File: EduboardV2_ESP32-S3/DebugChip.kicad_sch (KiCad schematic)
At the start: 31 parts, among them Q1 L8050QLT1G, Q2 L8050QLT1G, Q3 AO3401A, U2 CP2102N-A02-GQFN28R

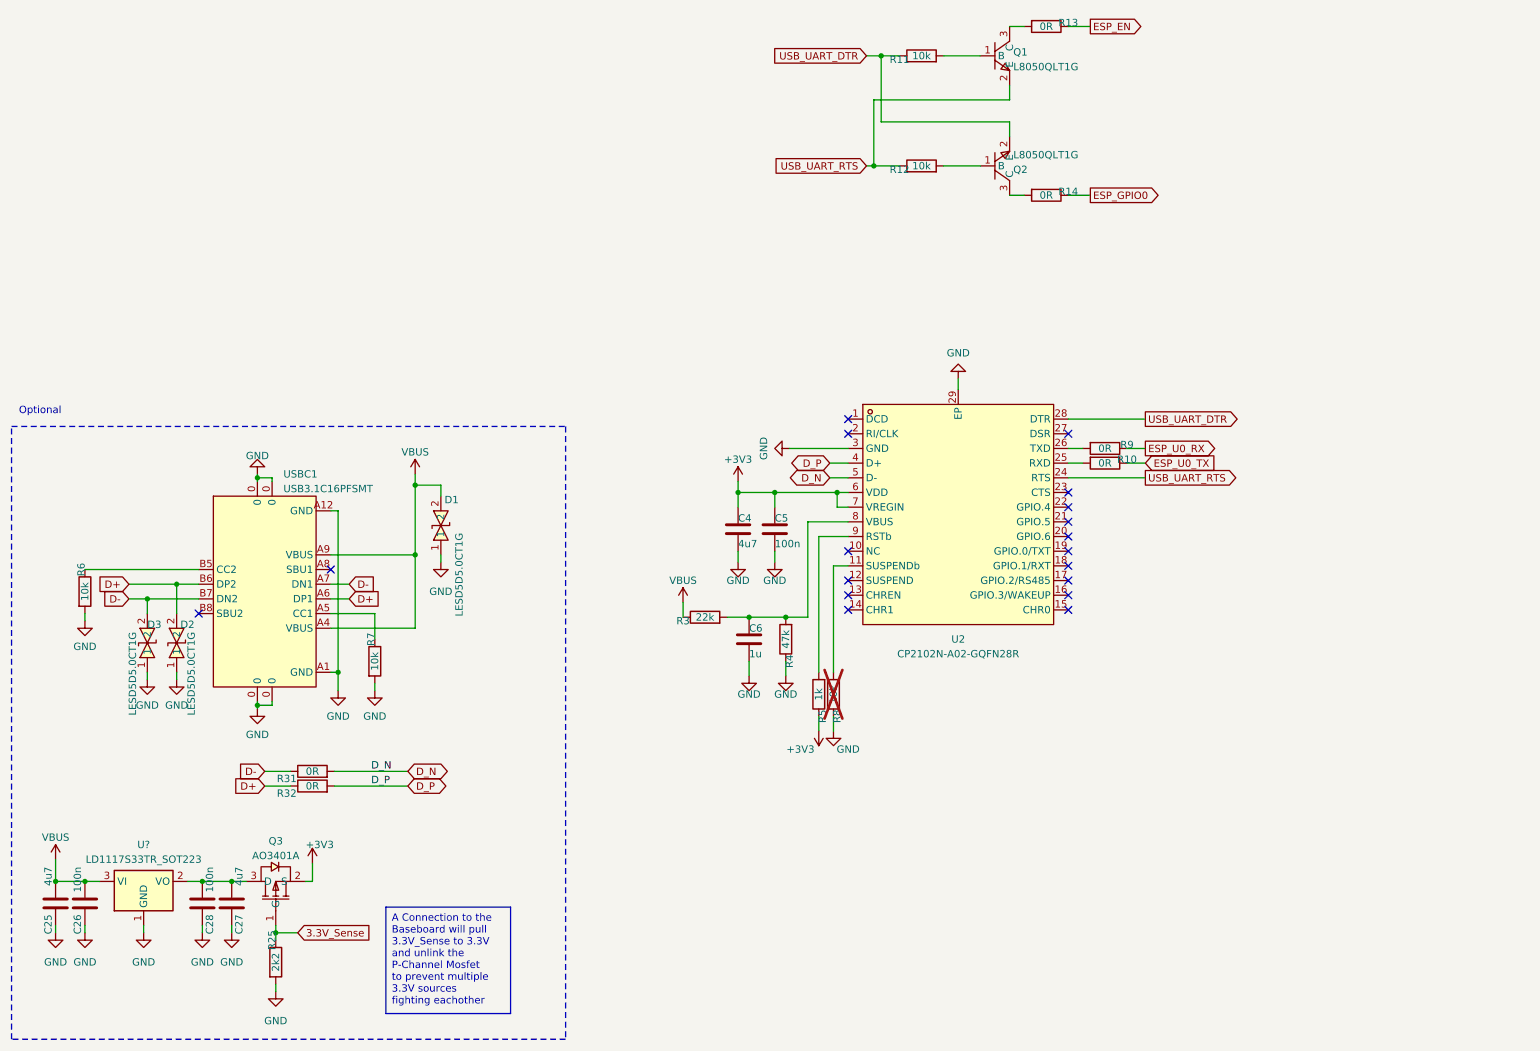
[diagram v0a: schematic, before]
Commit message: distribute signals to pins
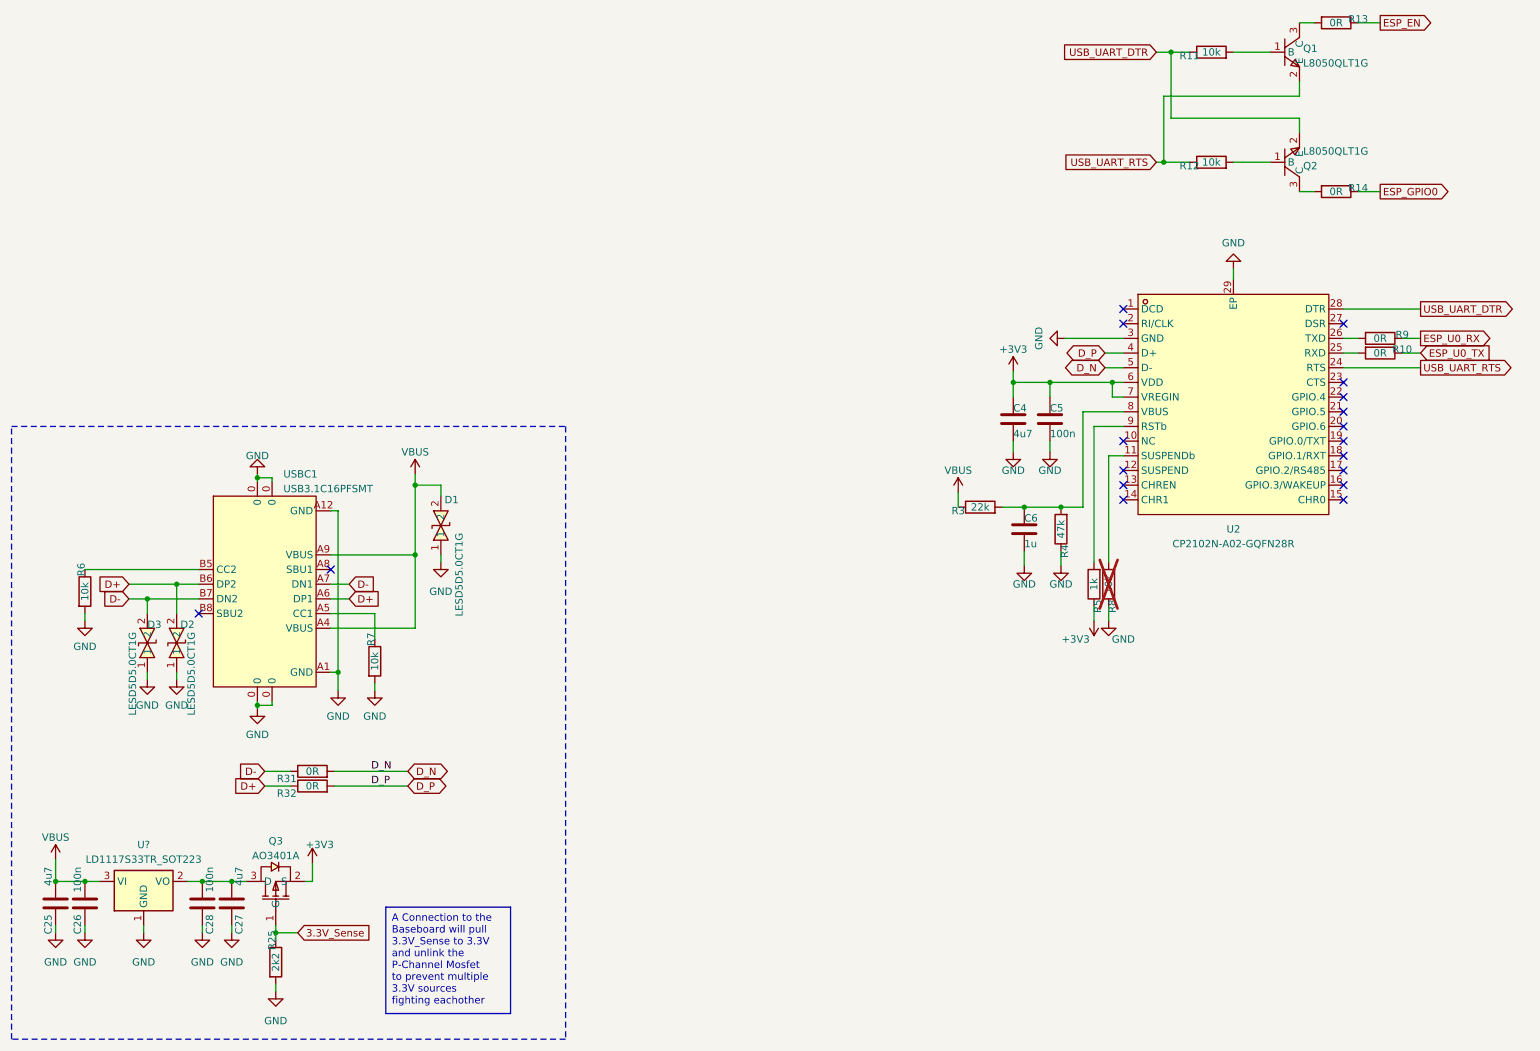
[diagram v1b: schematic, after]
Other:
- note removed: "Optional"
- moved on the sheet: C4, C5, C6, Q1, Q2, R10, R11, R12, R13, R14, R3, R4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

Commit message: finish schematic. Do Layout
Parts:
- removed R5: 1k, Resistor_SMD:R_0603_1608Metric, symbol Device:R
- added R1: 2k2, Resistor_SMD:R_0402_1005Metric, symbol Device:R
- C6: JLCPCB Part # (none) -> C77083; LCSC Part (none) -> C77083
- Q1, Q2: JLCPCB Part # (none) -> C49581
- R10, R13, R14, R9: footprint Resistor_SMD:R_0603_1608Metric -> Resistor_SMD:R_0402_1005Metric; JLCPCB Part # (none) -> C140225; LCSC Part (none) -> C140225
- R11, R12, R8: footprint Resistor_SMD:R_0603_1608Metric -> Resistor_SMD:R_0402_1005Metric; JLCPCB Part # (none) -> C71617; LCSC Part (none) -> C71617
- R25: footprint Resistor_SMD:R_0603_1608Metric -> Resistor_SMD:R_0402_1005Metric; JLCPCB Part # C115003 -> C114762; LCSC Part C115003 -> C114762
- R3: footprint Resistor_SMD:R_0603_1608Metric -> Resistor_SMD:R_0402_1005Metric; JLCPCB Part # (none) -> C144778; LCSC Part (none) -> C144778
- R31, R32: footprint Resistor_SMD:R_0603_1608Metric -> Resistor_SMD:R_0402_1005Metric; JLCPCB Part # C465460 -> C140225; LCSC Part C465460 -> C140225
- R4: footprint Resistor_SMD:R_0603_1608Metric -> Resistor_SMD:R_0402_1005Metric; JLCPCB Part # (none) -> C328320; LCSC Part (none) -> C328320
- R6, R7: footprint Resistor_SMD:R_0603_1608Metric -> Resistor_SMD:R_0402_1005Metric; JLCPCB Part # C116677 -> C71617; LCSC Part C116677 -> C71617
- U2: footprint easyeda2kicad:QFN-28_L5.0-W5.0-P0.50-TL-EP3.3 -> EduboardV2_kicadlib:QFN-28_L5.0-W5.0-P0.50-TL-EP3.3; JLCPCB Part # (none) -> C964632
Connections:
- net +3V3: now also R1.2
- net at U2.9 (RSTb): now also R1.1

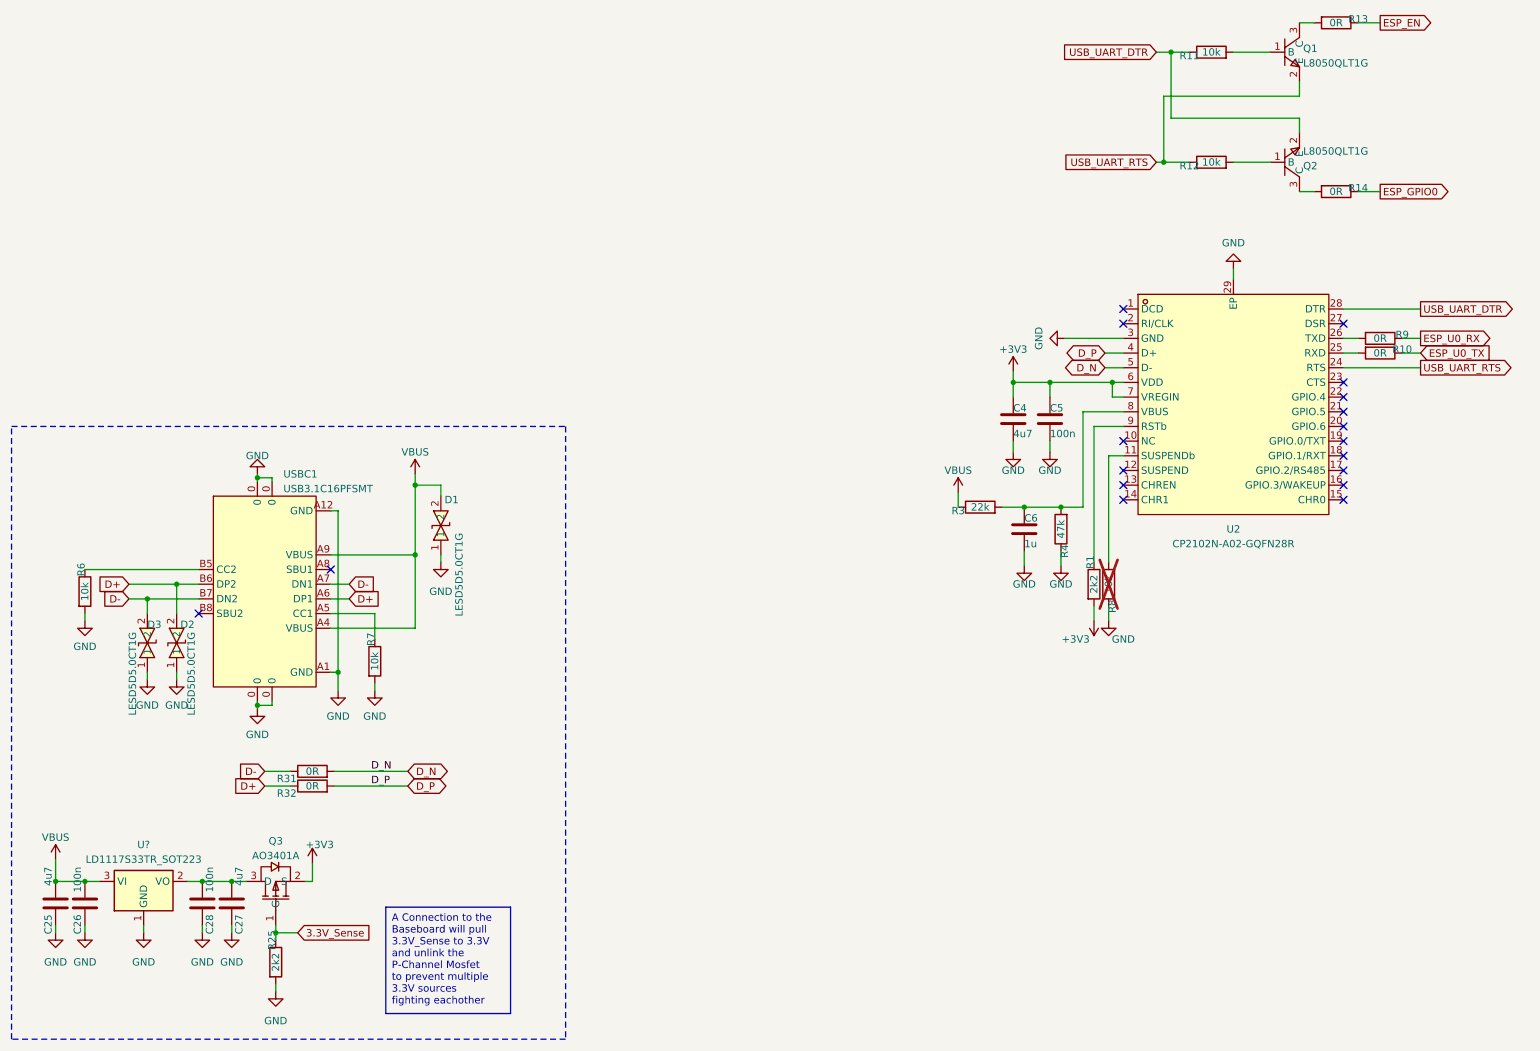
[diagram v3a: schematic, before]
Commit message: Do all modifications for V1.1 and create production data
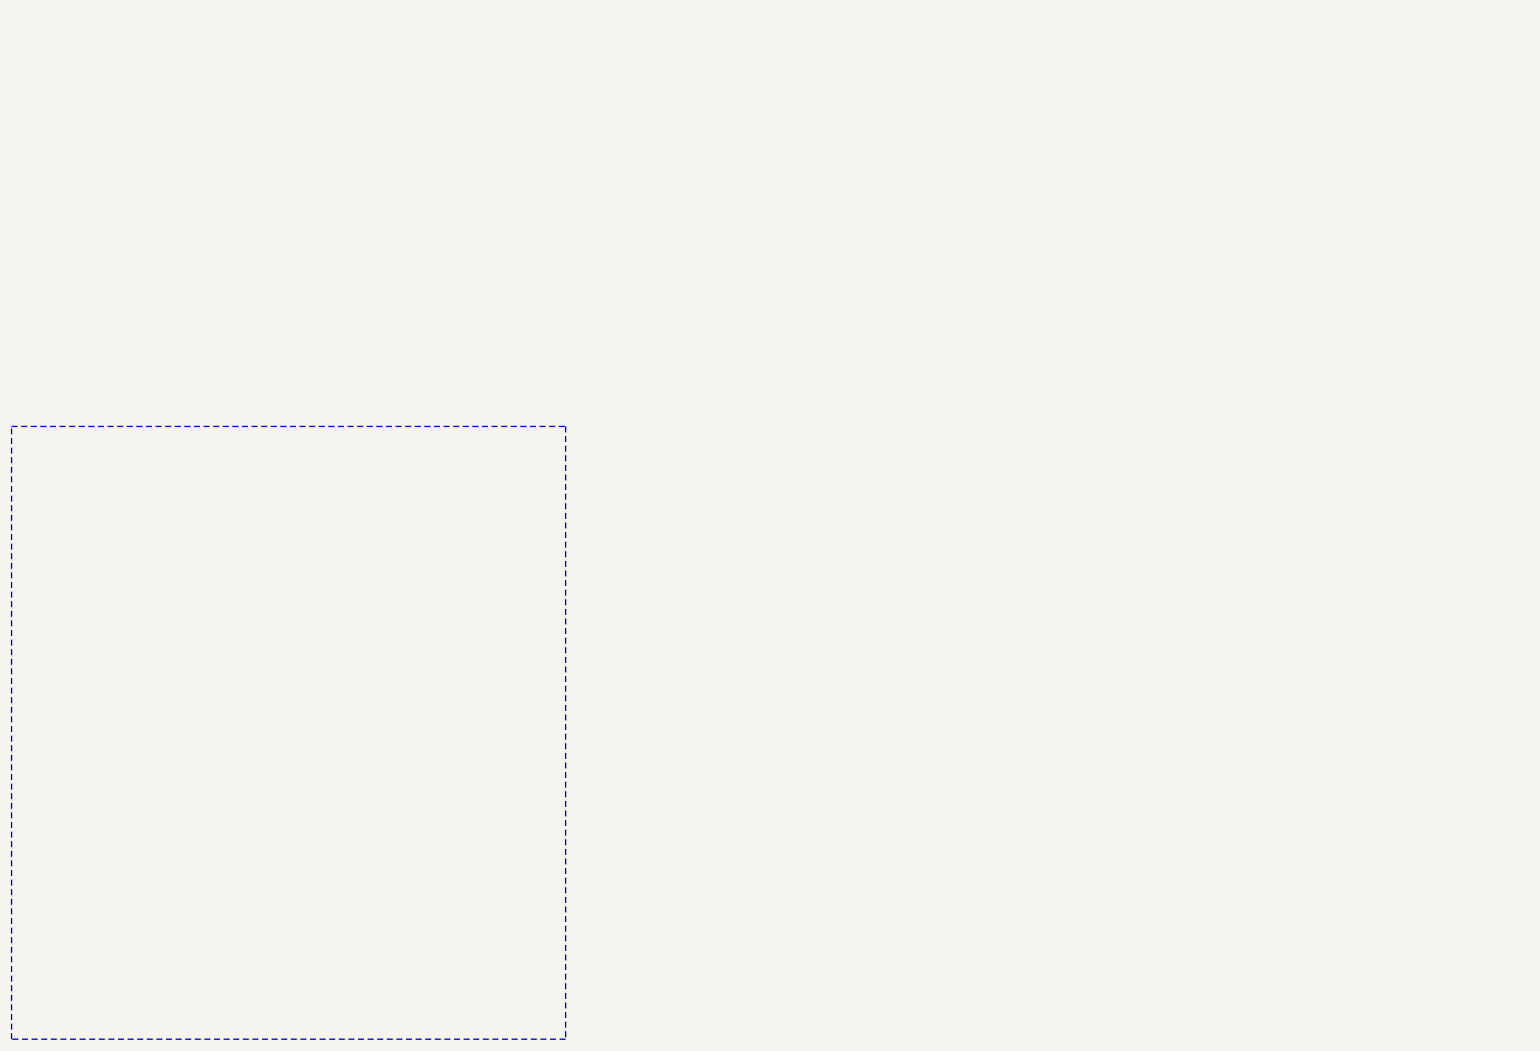
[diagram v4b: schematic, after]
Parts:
- removed C25, C27, C4: 4u7, Capacitor_SMD:C_0805_2012Metric, symbol Device:C
- removed C26, C28, C5: 100n, Capacitor_SMD:C_0603_1608Metric, symbol Device:C
- removed C6: 1u, Capacitor_SMD:C_0805_2012Metric, symbol Device:C
- removed D1, D2, D3: LESD5D5.0CT1G, EduboardV2_kicadlib:SOD-523_L1.2-W0.8-LS1.6-BI, symbol EduboardV2_kicadlib:LESD5D5.0CT1G
- removed Q1, Q2: L8050QLT1G, EduboardV2_kicadlib:SOT-23-3_L2.9-W1.3-P1.90-LS2.4-BR, symbol EduboardV2_kicadlib:L8050QLT1G
- removed Q3: AO3401A, EduboardV2_kicadlib:SOT-23_L2.9-W1.3-P1.90-LS2.4-BR, symbol EduboardV2_kicadlib:AO3401A
- removed R1, R25: 2k2, Resistor_SMD:R_0402_1005Metric, symbol Device:R
- removed R10, R13, R14, R31, R32, R9: 0R, Resistor_SMD:R_0402_1005Metric, symbol Device:R
- removed R11, R12, R6, R7, R8: 10k, Resistor_SMD:R_0402_1005Metric, symbol Device:R
- removed R3: 22k, Resistor_SMD:R_0402_1005Metric, symbol Device:R
- removed R4: 47k, Resistor_SMD:R_0402_1005Metric, symbol Device:R
- removed U2: CP2102N-A02-GQFN28R, EduboardV2_kicadlib:QFN-28_L5.0-W5.0-P0.50-TL-EP3.3, symbol EduboardV2_kicadlib:CP2102N-A02-GQFN28R
- removed U?: LD1117S33TR_SOT223, Package_TO_SOT_SMD:SOT-223-3_TabPin2, symbol Regulator_Linear:LD1117S33TR_SOT223
- removed USBC1: USB3.1C16PFSMT, EduboardV2_kicadlib:USB-C-SMD_TYPE-C-USB-17, symbol EduboardV2_kicadlib:USB3.1C16PFSMT
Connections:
- no-connect marks 18 -> 0
